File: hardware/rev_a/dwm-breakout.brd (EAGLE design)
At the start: 35.3 x 41.3 mm, 13 parts, among them J1 TC2030-JLINK-L

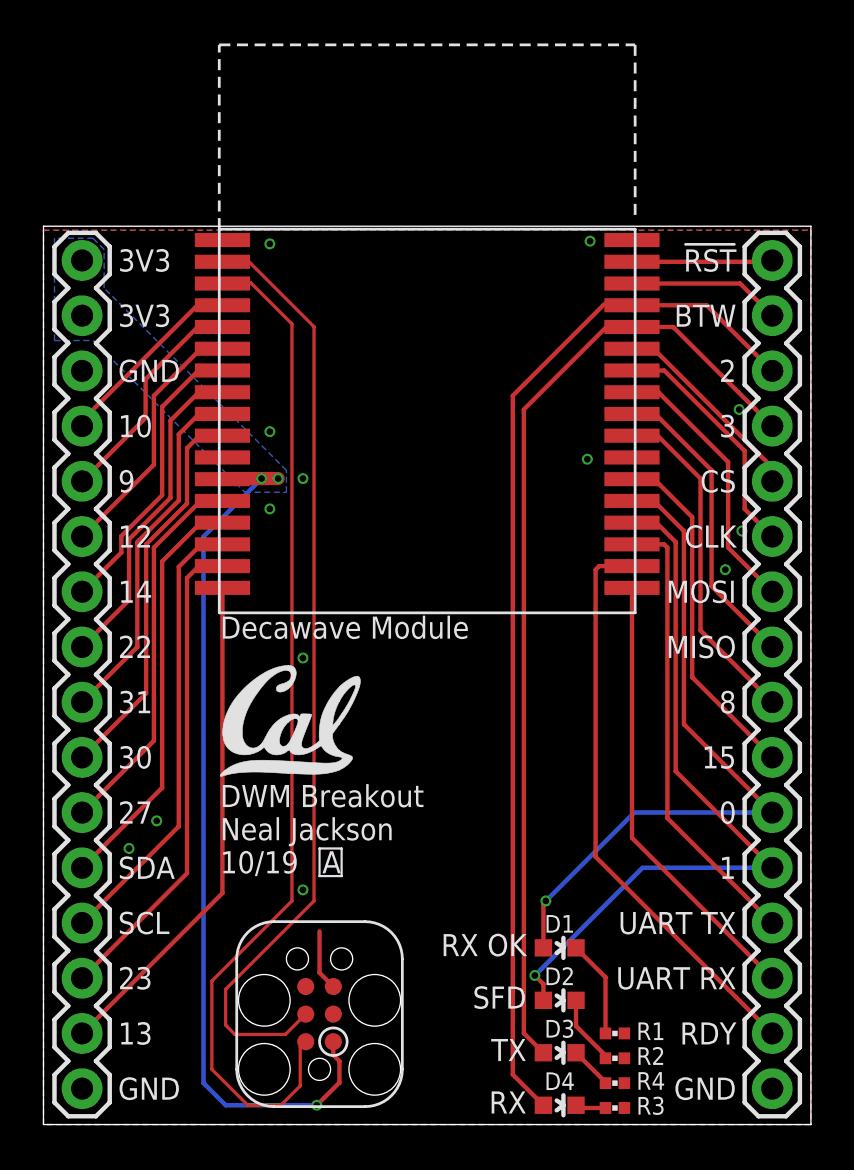
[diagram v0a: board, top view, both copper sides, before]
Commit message: Move LED+resistors
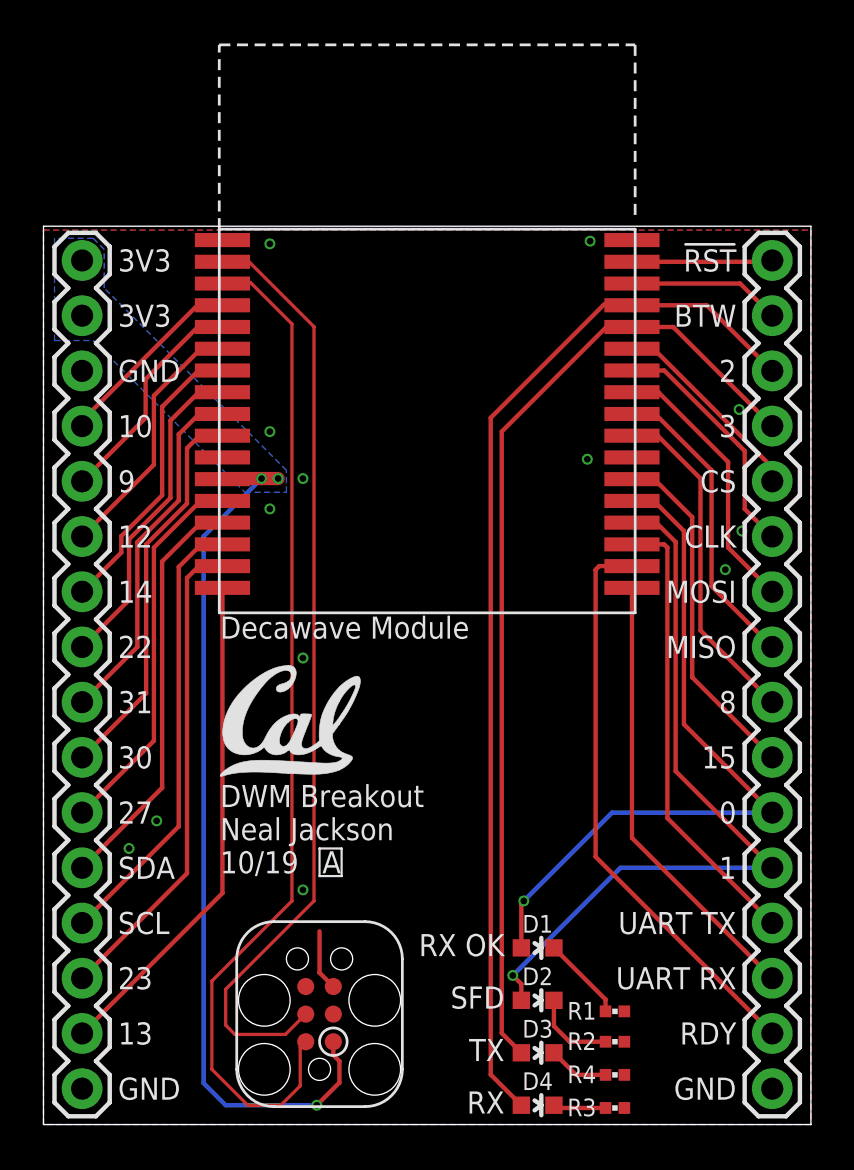
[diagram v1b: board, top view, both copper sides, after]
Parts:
- moved R1 1.02 mm to (26.3, 5.21)
- moved D1 1.02 mm to (22.7, 8.13)
- moved D2 1.02 mm to (22.7, 5.71)
- moved D3 1.02 mm to (22.7, 3.30)
- moved D4 1.02 mm to (22.7, 0.89)
- moved R2 0.76 mm to (26.3, 3.81)
- moved R4 0.38 mm to (26.3, 2.29)
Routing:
- net SFDLED: track 33.5 -> 34.5 mm
- net RXOKLED: track 31.9 -> 32.9 mm
- net N$7: track 1.41 -> 2.43 mm
- net N$8: track 1.96 -> 2.79 mm
- net N$6: track 3.23 -> 3.86 mm
- net N$1: track 4.50 -> 3.90 mm
